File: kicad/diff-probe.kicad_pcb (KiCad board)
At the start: 2 copper layers, 49.2 x 20.5 mm, 30 parts, among them IC3 LMH6702, IC4 LMH6702, IC5 LMH6702, J3 HEADER-1X2CARD-EDGE, J4 Molex 502494-0470, X2 SMA--BU-SMA-H

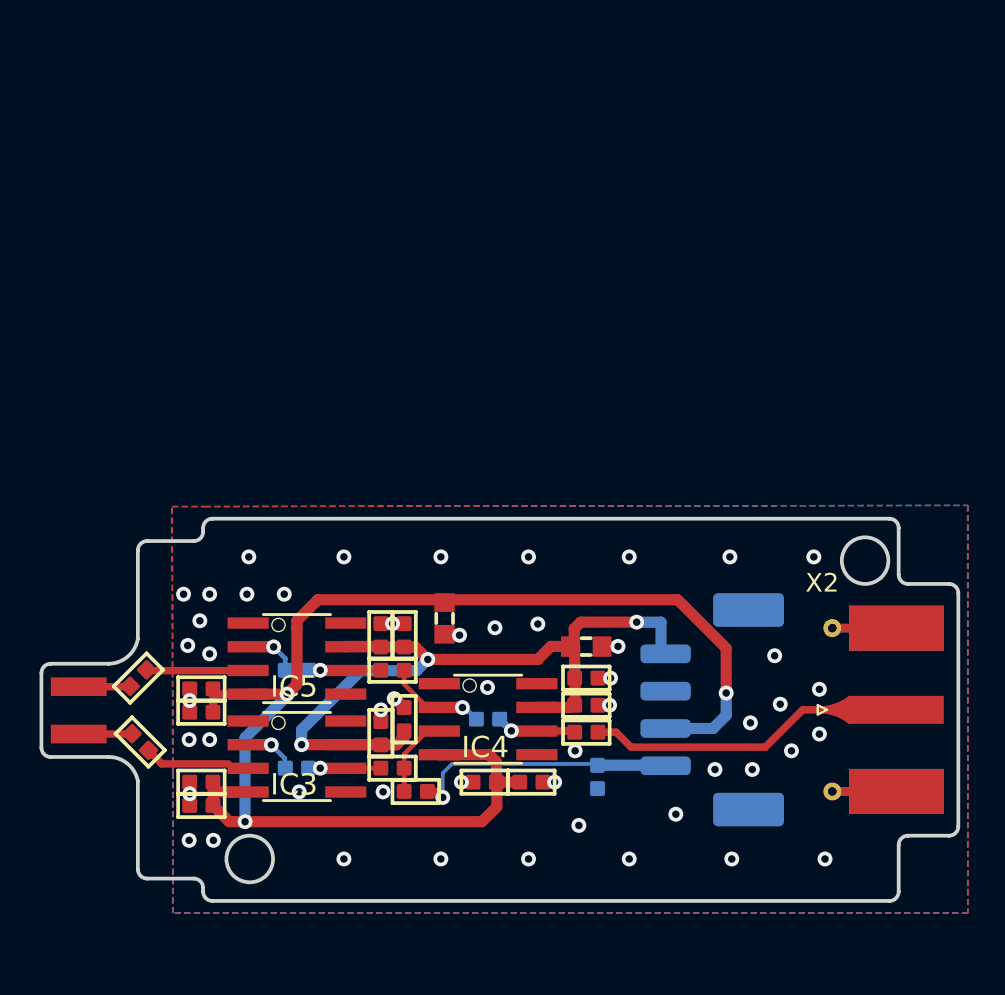
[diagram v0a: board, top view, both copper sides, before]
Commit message: Change name for the old project to the kicad_old, remove old stored files. Create new design use new faster op-amp, and two op-amp differential input, create simulation for it. Update PCB design. Still need to design the PCB file, and check the simulation result - need some optimization.
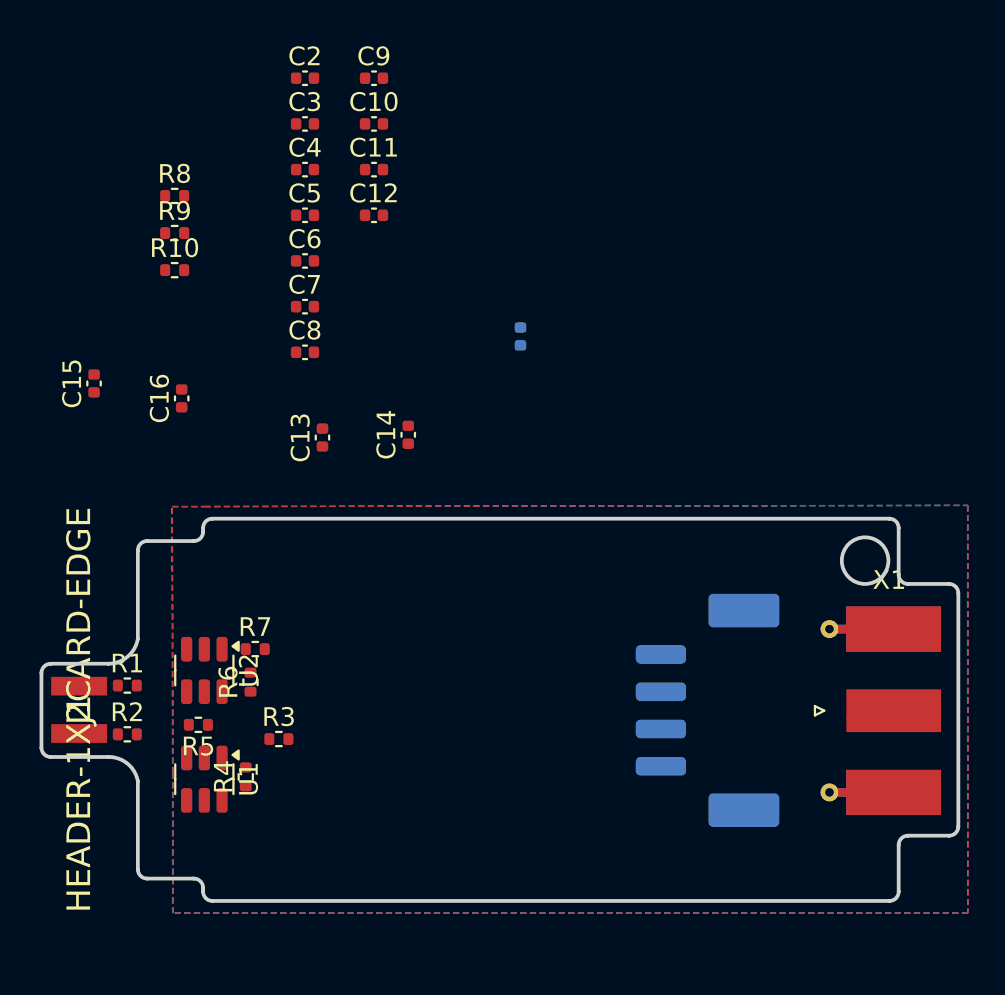
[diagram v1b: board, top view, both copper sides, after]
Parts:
- removed C17, C18, C19, C20, C21, C22, C23, C24: 100nF, Library:0402-SQUARE
- removed C52, C54: 1µF, Library:0603
- removed IC3, IC4, IC5: LMH6702, Library:SO08
- removed J4: Molex 502494-0470, Connector_Molex:Molex_CLIK-Mate_502494-0470_1x04-1MP_P2.00mm_Horizontal
- removed R20, R28: 150Ω, Library:0402-SQUARE
- removed R22, R32: 1.1kΩ, Library:0402-SQUARE
- removed R26, R27, R37, R38: 220Ω, Library:0402-SQUARE
- removed R30: 50Ω, Library:0402-SQUARE
- removed X2: SMA--BU-SMA-H, Connector_Coaxial:SMA_Molex_73251-1153_EdgeMount_Horizontal_new
- added C10: 100nF, Capacitor_SMD:C_0402_1005Metric, F.Cu at (142.5, 66.6)
- added C11: 100nF, Capacitor_SMD:C_0402_1005Metric, F.Cu at (142.5, 69.0)
- added C12: 100nF, Capacitor_SMD:C_0402_1005Metric, F.Cu at (142.5, 71.5)
- added C2: 100nF, Capacitor_SMD:C_0402_1005Metric, F.Cu at (138.8, 64.1)
- added C3: 100nF, Capacitor_SMD:C_0402_1005Metric, F.Cu at (138.8, 66.6)
- added C4: 100nF, Capacitor_SMD:C_0402_1005Metric, F.Cu at (138.8, 69.0)
- added C5: 100nF, Capacitor_SMD:C_0402_1005Metric, F.Cu at (138.8, 71.5)
- added C6: 100nF, Capacitor_SMD:C_0402_1005Metric, F.Cu at (138.8, 73.9)
- added C7: 100nF, Capacitor_SMD:C_0402_1005Metric, F.Cu at (138.8, 76.4)
- added C8: 100nF, Capacitor_SMD:C_0402_1005Metric, F.Cu at (138.8, 78.8)
- added C9: 100nF, Capacitor_SMD:C_0402_1005Metric, F.Cu at (142.5, 64.1)
- added J1: HEADER-1X2CARD-EDGE, Library:CARD_EDGE_PADS-1X2, F.Cu at (126.7, 98.0)
- added R1: 100Ω, Resistor_SMD:R_0402_1005Metric, F.Cu at (129.3, 96.7)
- added R10: 1kΩ, Resistor_SMD:R_0402_1005Metric, F.Cu at (131.8, 74.4)
- added R2: 100, Resistor_SMD:R_0402_1005Metric, F.Cu at (129.3, 99.3)
- added R3: 10kΩ, Resistor_SMD:R_0402_1005Metric, F.Cu at (137.4, 99.6)
- added R4: 10kΩ, Resistor_SMD:R_0402_1005Metric, F.Cu at (135.6, 101.6)
- added R5: 10kΩ, Resistor_SMD:R_0402_1005Metric, F.Cu at (133.1, 98.8)
- added R6: 10kΩ, Resistor_SMD:R_0402_1005Metric, F.Cu at (135.9, 96.5)
- added R7: 50Ω, Resistor_SMD:R_0402_1005Metric, F.Cu at (136.1, 94.7)
- added R8: 50Ω, Resistor_SMD:R_0402_1005Metric, F.Cu at (131.8, 70.4)
- added R9: 99kΩ, Resistor_SMD:R_0402_1005Metric, F.Cu at (131.8, 72.4)
- added U1: OPA847xDBV, Package_TO_SOT_SMD:SOT-23-6, F.Cu at (133.4, 101.7)
- added U2: OPA847xDBV, Package_TO_SOT_SMD:SOT-23-6, F.Cu at (133.4, 95.9)
- added X1: SMA--BU-SMA-H, Connector_Coaxial:SMA_Molex_73251-1153_EdgeMount_Horizontal, F.Cu at (168.7, 98.0)
- C1, C16: footprint Library:0402-SQUARE -> Capacitor_SMD:C_0402_1005Metric
- C13: value 100nF -> 1nF; footprint Library:0402-SQUARE -> Capacitor_SMD:C_0402_1005Metric
- C14, C15: value 100nF -> 1µF; footprint Library:0402-SQUARE -> Capacitor_SMD:C_0402_1005Metric
- J3: value HEADER-1X2CARD-EDGE -> Molex 502494-0470; footprint Library:CARD_EDGE_PADS-1X2 -> Connector_Molex:Molex_CLIK-Mate_502494-0470_1x04-1MP_P2.00mm_Horizontal; moved to B.Cu
- moved J3 33.7 mm to (160.4, 98.0), turned to -90 degrees
- moved C15 24.5 mm to (127.5, 80.5)
- moved C1 24.0 mm to (150.4, 78.0)
- moved C16 20.9 mm to (132.2, 81.3)
- moved C13 11.1 mm to (139.8, 83.4)
- moved C14 10.8 mm to (144.3, 83.2)
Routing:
- net V-: track 84.5 -> 0.00 mm, vias 3 -> 0
- net V+: track 41.2 -> 0.00 mm, vias 3 -> 0
- net GND: track 23.8 -> 0.00 mm, vias 51 -> 0
- net /OutPad: track 17.2 -> 0.00 mm
- net /offset: track 14.6 -> 0.00 mm, vias 1 -> 0
- net /NEGIN: track 6.65 -> 0.00 mm
- net /NEGMID: track 6.58 -> 0.00 mm, vias 1 -> 0
- net /POSMID: track 5.16 -> 0.00 mm
- net /OUT: track 4.66 -> 0.00 mm, vias 1 -> 0
- net /POSIN: track 4.61 -> 0.00 mm
- net /NegIn1: track 3.94 -> 0.00 mm, vias 1 -> 0
- net /PosIn1: track 3.89 -> 0.00 mm, vias 1 -> 0
- net Net-(IC5-Pad2): track 2.88 -> 0.00 mm, vias 1 -> 0
- net Net-(IC3-Pad2): track 2.83 -> 0.00 mm, vias 1 -> 0
- net /PosPad: track 2.86 -> 0.04 mm
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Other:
- outline, holes or cut-outs redrawn
- rule pad_to_mask_clearance: 0 -> 0.1
- board text removed: "0.2000 mm / 0.1778 mm"
- board text removed: "0.3000 mm"
- board text removed: "1.6000 mm"
- board text removed: "2"
- board text removed: "49.1709 mm x 20.5000 mm"
- board text removed: "BOARD CHARACTERISTICS"
- board text removed: "Board Thickness:"
- board text removed: "Board overall dimensions:"
- board text removed: "Castellated pads:"
- board text removed: "Copper Finish:"
- board text removed: "Copper Layer Count:"
- board text removed: "ENIG"
- board text removed: "Edge card connectors:"
- board text removed: "Impedance Control:"
- board text removed: "Min hole diameter:"
- board text removed: "Min track/spacing:"
- board text removed: "No"
- board text removed: "Plated Board Edge:"
- board text removed: "Yes"

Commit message: Update schematic using the new version of Op-amp, with high bandwidth, new topology, new DC/DC converter to create 5V power supply from 15V, and negative -5V from it.
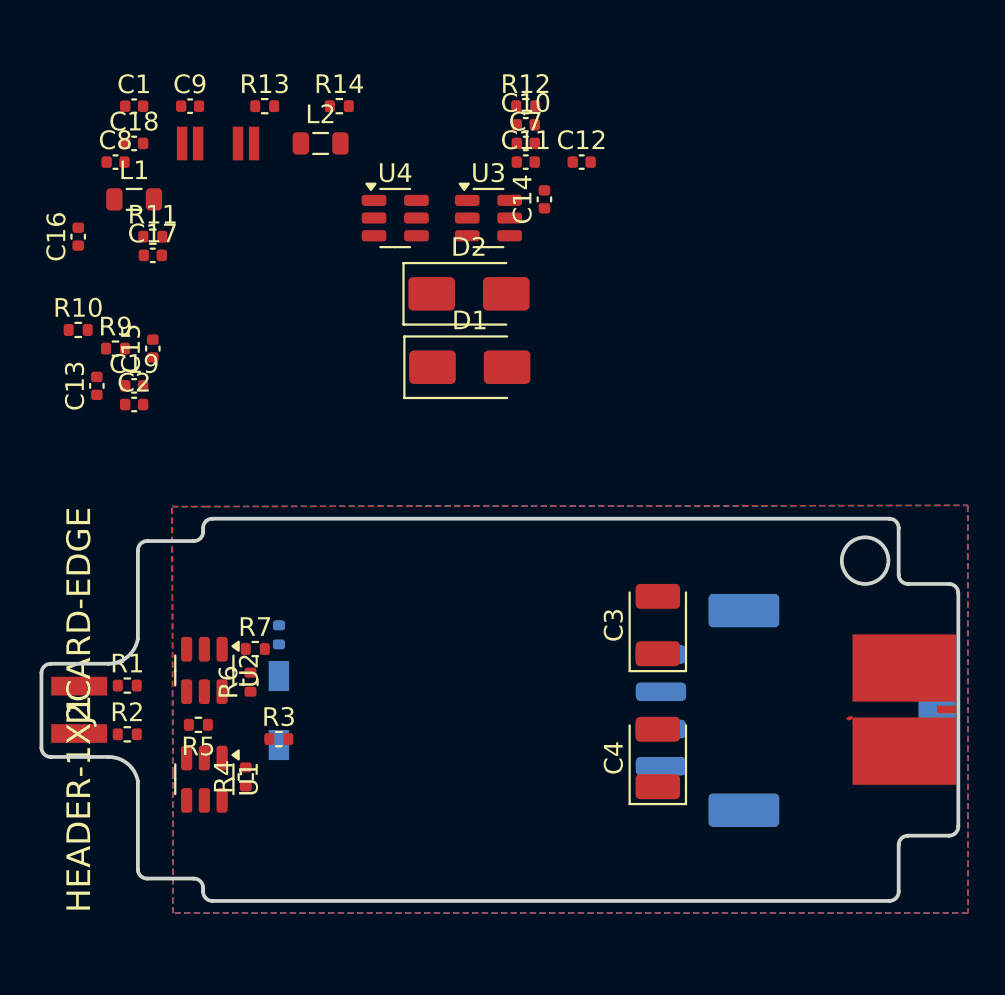
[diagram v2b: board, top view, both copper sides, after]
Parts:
- removed R8: 50Ω, Resistor_SMD:R_0402_1005Metric
- added C17: 10nF, Capacitor_SMD:C_0402_1005Metric, F.Cu at (130.7, 73.6)
- added C18: 10uF/6.3V, Capacitor_SMD:C_0402_1005Metric, F.Cu at (129.7, 67.6)
- added C19: 10uF/16V, Capacitor_SMD:C_0402_1005Metric, F.Cu at (129.7, 80.6)
- added D1: SS13A, Diode_SMD:D_SMA, F.Cu at (147.7, 79.6)
- added D2: SS13A, Diode_SMD:D_SMA, F.Cu at (147.6, 75.7)
- added D3: OSM44008C1F, LED_SMD:LED_OptoSupply_OSXX4008C1F_4x1.4mm_Horizontal, B.Cu at (137.4, 98.0)
- added L1: 4.7uH, Inductor_SMD:L_0805_2012Metric, F.Cu at (129.7, 70.6)
- added L2: 4.7uH, Inductor_SMD:L_0805_2012Metric, F.Cu at (139.7, 67.6)
- added R11: 24kΩ, Resistor_SMD:R_0402_1005Metric, F.Cu at (130.7, 72.6)
- added R12: 4.7kΩ, Resistor_SMD:R_0402_1005Metric, F.Cu at (150.7, 65.6)
- added R13: 24kΩ, Resistor_SMD:R_0402_1005Metric, F.Cu at (136.7, 65.6)
- added R14: 4.7kΩ, Resistor_SMD:R_0402_1005Metric, F.Cu at (140.7, 65.6)
- added R26: 1k, Resistor_SMD:R_0402_1005Metric, B.Cu at (137.4, 94.0)
- added U3: AP3211K, Package_TO_SOT_SMD:SOT-23-6, F.Cu at (148.7, 71.6)
- added U4: AP3211K, Package_TO_SOT_SMD:SOT-23-6, F.Cu at (143.7, 71.6)
- C1: moved to F.Cu
- C12: value 100nF -> 1µF
- C3, C4: value 100nF -> 22uF; footprint Capacitor_SMD:C_0402_1005Metric -> Capacitor_Tantalum_SMD:CP_EIA-3528-21_Kemet-B
- C5, C6: footprint Capacitor_SMD:C_0402_1005Metric -> Capacitor_SMD:C_0306_0816Metric
- C7: value 100nF -> 10uF/16V
- C8: value 100nF -> 10nF
- C9: value 100nF -> 10uF/6.3V
- R3, R4, R5, R6: value 10kΩ -> 1kΩ
- R7: value 50Ω -> 10Ω
- X1: value SMA--BU-SMA-H -> 901-10511-3; footprint Connector_Coaxial:SMA_Molex_73251-1153_EdgeMount_Horizontal -> Connector_Coaxial:901-10511-3
- moved C4 36.8 mm to (157.7, 100.6), turned to 90 degrees
- moved C3 32.9 mm to (157.7, 93.5), turned to 90 degrees
- moved C1 24.1 mm to (129.7, 65.6), turned to 0 degrees
- moved C2 19.8 mm to (129.7, 81.6)
- moved C7 14.7 mm to (150.7, 67.6)
- moved C14 14.6 mm to (151.7, 70.6)
- moved C8 14.4 mm to (128.7, 68.6)
- moved C13 12.4 mm to (127.7, 80.6)
- moved C12 11.5 mm to (153.7, 68.6)
- moved C16 10.3 mm to (126.7, 72.6)
- moved C9 9.98 mm to (132.7, 65.6)
- moved C6 8.81 mm to (132.7, 67.6)
- moved C11 8.15 mm to (150.7, 68.6)
- moved C10 8.14 mm to (150.7, 66.6)
- moved R9 6.96 mm to (128.7, 78.6)
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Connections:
- C10 pad 1: (no net) -> Net-(C10-Pad1)
- C10 pad 2: (no net) -> GND
- C11 pad 1: (no net) -> Net-(C10-Pad1)
- C11 pad 2: (no net) -> GND
- C12 pad 1: (no net) -> /Power_supply/IN_P
- C12 pad 2: (no net) -> /Power_supply/OUT_N
- C14 pad 1: Net-(C1-1) -> /Power_supply/IN_P
- C15 pad 2: Net-(C10-2) -> /Power_supply/IN_N
- C3 pad 1: (no net) -> /Power_supply/IN_P
- C3 pad 2: (no net) -> GND
- C4 pad 1: (no net) -> GND
- C4 pad 2: (no net) -> /Power_supply/IN_N
- C5 pad 1: (no net) -> GND
- C5 pad 2: (no net) -> /Power_supply/OUT_N
- C6 pad 1: (no net) -> /Power_supply/OUT_P
- C6 pad 2: (no net) -> GND
- C7 pad 1: (no net) -> /Power_supply/IN_P
- C7 pad 2: (no net) -> GND
- C8 pad 1: (no net) -> Net-(U3-SW)
- C8 pad 2: (no net) -> Net-(D1-K)
- C9 pad 1: (no net) -> /Power_supply/OUT_P
- C9 pad 2: (no net) -> GND
- J3 pad 1: Net-(C1-1) -> /Power_supply/IN_P
- J3 pad 3: Net-(C10-2) -> /Power_supply/IN_N

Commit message: New version at the end of the day.
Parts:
- removed C11: 100nF, Capacitor_SMD:C_0402_1005Metric
- removed X1: 901-10511-3, Connector_Coaxial:901-10511-3
- added J4: 901-10511-3, Connector_Coaxial:901-10511-3, F.Cu at (173.7, 98.0)
- moved C16 44.1 mm to (158.0, 103.6), turned to 0 degrees
- moved C15 38.0 mm to (162.1, 100.1)
- moved C18 37.9 mm to (148.3, 100.6), turned to -90 degrees
- moved R10 37.4 mm to (155.2, 101.9), turned to 90 degrees
- moved C5 37.4 mm to (132.8, 104.9), turned to 90 degrees
- moved R9 36.8 mm to (156.7, 102.4), turned to 180 degrees
- moved R14 36.0 mm to (149.4, 100.6), turned to -90 degrees
- moved R13 35.6 mm to (148.8, 99.1)
- moved C8 34.9 mm to (155.4, 90.9), turned to 180 degrees
- moved C19 33.8 mm to (157.0, 100.6), turned to -90 degrees
- moved C17 33.1 mm to (155.4, 95.5), turned to 180 degrees
- moved C12 31.5 mm to (155.4, 100.1), turned to 180 degrees
- moved L2 30.6 mm to (148.8, 96.8), turned to -90 degrees
- moved C9 30.1 mm to (147.3, 91.9), turned to -90 degrees
- moved C7 29.9 mm to (162.6, 95.0)
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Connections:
- C1 pad 1: (no net) -> /Power_supply/V+
- C1 pad 2: (no net) -> GND
- C12 pad 2: /Power_supply/OUT_N -> /Power_supply/V-
- C13 pad 1: (no net) -> /offset_prec
- C13 pad 2: (no net) -> GND
- C16 pad 1: (no net) -> /offset
- C16 pad 2: (no net) -> GND
- C18 pad 2: /Power_supply/OUT_N -> /Power_supply/V-
- C2 pad 1: (no net) -> GND
- C2 pad 2: (no net) -> /Power_supply/V-
- C5 pad 2: /Power_supply/OUT_N -> /Power_supply/V-
- C6 pad 1: /Power_supply/OUT_P -> /Power_supply/V+
- C9 pad 1: /Power_supply/OUT_P -> /Power_supply/V+
- D2 pad 2: /Power_supply/OUT_N -> /Power_supply/V-
- L1 pad 2: /Power_supply/OUT_P -> /Power_supply/V+
- R11 pad 1: /Power_supply/OUT_P -> /Power_supply/V+
- R14 pad 2: /Power_supply/OUT_N -> /Power_supply/V-
- U4 pad 2: /Power_supply/OUT_N -> /Power_supply/V-
